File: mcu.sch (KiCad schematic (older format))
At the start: 16 parts, among them SW3 SW_PUSH, U1 STM32F411RE_LQFP64, X1 32.768K, X2 8MHz

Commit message: Began layout
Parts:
- removed C1, C2: 10pF, Capacitors_SMD:C_0805_HandSoldering, symbol C
- removed X1: 32.768K, Crystals:Crystal_HC49-SD_SMD, symbol CRYSTAL
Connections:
- wire segments 111 -> 103
- no-connect marks 17 -> 19
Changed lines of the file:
@@
 USART_RX
-$Comp
-L CRYSTAL X1
-U 1 1 5430D2CD
-P 3150 1850
-F 0 "X1" H 3150 2000 60  0000 C CNN
-F 1 "32.768K" H 3150 1700 60  0000 C CNN
-F 2 "Crystals:Crystal_HC49-SD_SMD" H 3150 1850 60  0001 C CNN
-F 3 "~" H 3150 1850 60  0000 C CNN
-	1    3150 1850
-	0    1    1    0
-$EndComp
 $Comp
 L CRYSTAL X2
@@
 	1    3150 2800
 	0    1    1    0
-$EndComp
-$Comp
-L C C1
-U 1 1 5430D3C7
-P 2750 1500
-F 0 "C1" H 2750 1600 40  0000 L CNN
-F 1 "10pF" H 2756 1415 40  0000 L CNN
-F 2 "Capacitors_SMD:C_0805_HandSoldering" H 2788 1350 30  0000 C CNN
-F 3 "~" H 2750 1500 60  0000 C CNN
-	1    2750 1500
-	0    -1   -1   0
-$EndComp
-$Comp
-L C C2
-U 1 1 5430D401
-P 2750 2200
-F 0 "C2" H 2750 2300 40  0000 L CNN
-F 1 "10pF" H 2756 2115 40  0000 L CNN
-F 2 "Capacitors_SMD:C_0805_HandSoldering" H 2788 2050 30  0000 C CNN
-F 3 "~" H 2750 2200 60  0000 C CNN
-	1    2750 2200
-	0    -1   -1   0
 $EndComp
 $Comp
@@
 Connection ~ 7500 3400
 Wire Wire Line
-	2500 1500 2500 3250
-Wire Wire Line
-	2500 1500 2550 1500
-Wire Wire Line
-	2550 2200 2500 2200
-Connection ~ 2500 2200
-Wire Wire Line
 	2550 2450 2500 2450
 Connection ~ 2500 2450
@@
 Wire Wire Line
 	3150 2450 2950 2450
-Wire Wire Line
-	2950 2200 4450 2200
-Wire Wire Line
-	3150 2200 3150 2150
-Wire Wire Line
-	3150 1550 3150 1500
-Wire Wire Line
-	2950 1500 3500 1500
-Wire Wire Line
-	4450 2100 3500 2100
-Wire Wire Line
-	3500 2100 3500 1500
-Connection ~ 3150 1500
-Connection ~ 3150 2200
 Wire Wire Line
 	4450 2300 3150 2300
@@
 Text HLabel 7050 2600 2    60   Input ~ 0
 TRIGGER4
+Wire Wire Line
+	2500 3150 2500 2450
+NoConn ~ 4450 2100
+NoConn ~ 4450 2200
 $EndSCHEMATC

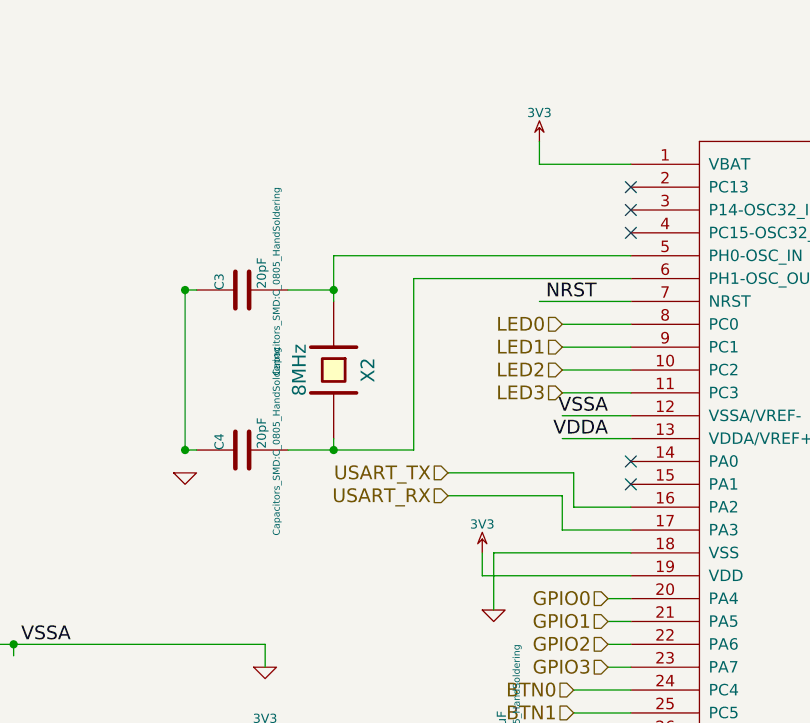
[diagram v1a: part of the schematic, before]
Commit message: New MOSFETs
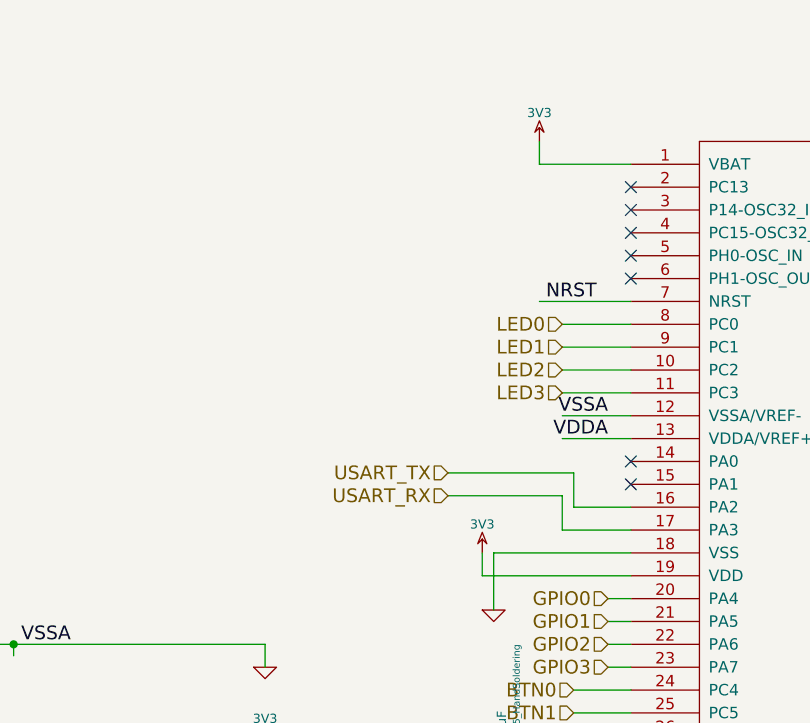
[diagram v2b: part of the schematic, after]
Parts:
- removed C3, C4: 20pF, Capacitors_SMD:C_0805_HandSoldering, symbol C
- removed X2: 8MHz, Crystals:Crystal_HC49-U_Vertical, symbol CRYSTAL
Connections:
- wire segments 103 -> 93
- no-connect marks 19 -> 21
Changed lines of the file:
@@
 LIBS:xbee
 LIBS:avbay-cache
-EELAYER 25 0
+EELAYER 27 0
 EELAYER END
 $Descr USLetter 11000 8500
@@
 Sheet 2 4
 Title "MCU"
-Date "4 dec 2014"
+Date "6 dec 2014"
 Rev ""
 Comp ""
@@
 $EndDescr
 $Comp
-L 3V3 #PWR08
+L 3V3 #PWR12
 U 1 1 542CDA8F
 P 3800 3600
-F 0 "#PWR08" H 3800 3700 40  0001 C CNN
+F 0 "#PWR12" H 3800 3700 40  0001 C CNN
 F 1 "3V3" H 3800 3725 40  0000 C CNN
 F 2 "" H 3800 3600 60  0000 C CNN
@@
 $EndComp
 $Comp
-L GND #PWR09
+L GND #PWR14
 U 1 1 542CDA9E
 P 3850 3850
-F 0 "#PWR09" H 3850 3850 30  0001 C CNN
+F 0 "#PWR14" H 3850 3850 30  0001 C CNN
 F 1 "GND" H 3850 3780 30  0001 C CNN
 F 2 "" H 3850 3850 60  0000 C CNN
@@
 $EndComp
 $Comp
-L 3V3 #PWR010
+L 3V3 #PWR13
 U 1 1 542CDAB1
 P 3800 4800
-F 0 "#PWR010" H 3800 4900 40  0001 C CNN
+F 0 "#PWR13" H 3800 4900 40  0001 C CNN
 F 1 "3V3" H 3800 4925 40  0000 C CNN
 F 2 "" H 3800 4800 60  0000 C CNN
@@
 $EndComp
 $Comp
-L 3V3 #PWR011
+L 3V3 #PWR22
 U 1 1 542CDAB7
 P 7450 4850
-F 0 "#PWR011" H 7450 4950 40  0001 C CNN
+F 0 "#PWR22" H 7450 4950 40  0001 C CNN
 F 1 "3V3" H 7450 4975 40  0000 C CNN
 F 2 "" H 7450 4850 60  0000 C CNN
@@
 $EndComp
 $Comp
-L 3V3 #PWR012
+L 3V3 #PWR23
 U 1 1 542CDC4D
 P 7500 3350
-F 0 "#PWR012" H 7500 3450 40  0001 C CNN
+F 0 "#PWR23" H 7500 3450 40  0001 C CNN
 F 1 "3V3" H 7500 3475 40  0000 C CNN
 F 2 "" H 7500 3350 60  0000 C CNN
@@
 Text HLabel 3650 3350 0    60   Input ~ 0
 USART_RX
-$Comp
-L CRYSTAL X2
-U 1 1 5430D2DC
-P 3150 2800
-F 0 "X2" H 3150 2950 60  0000 C CNN
-F 1 "8MHz" H 3150 2650 60  0000 C CNN
-F 2 "Crystals:Crystal_HC49-U_Vertical" H 3150 2800 60  0001 C CNN
-F 3 "~" H 3150 2800 60  0000 C CNN
-	1    3150 2800
-	0    1    1    0
-$EndComp
-$Comp
-L C C3
-U 1 1 5430D41B
-P 2750 2450
-F 0 "C3" H 2750 2550 40  0000 L CNN
-F 1 "20pF" H 2756 2365 40  0000 L CNN
-F 2 "Capacitors_SMD:C_0805_HandSoldering" H 2788 2300 30  0000 C CNN
-F 3 "~" H 2750 2450 60  0000 C CNN
-	1    2750 2450
-	0    -1   -1   0
-$EndComp
-$Comp
-L C C4
-U 1 1 5430D441
-P 2750 3150
-F 0 "C4" H 2750 3250 40  0000 L CNN
-F 1 "20pF" H 2756 3065 40  0000 L CNN
-F 2 "Capacitors_SMD:C_0805_HandSoldering" H 2788 3000 30  0000 C CNN
-F 3 "~" H 2750 3150 60  0000 C CNN
-	1    2750 3150
-	0    -1   -1   0
-$EndComp
-$Comp
-L GND #PWR013
-U 1 1 5430D447
-P 2500 3250
-F 0 "#PWR013" H 2500 3250 30  0001 C CNN
-F 1 "GND" H 2500 3180 30  0001 C CNN
-F 2 "" H 2500 3250 60  0000 C CNN
-F 3 "" H 2500 3250 60  0000 C CNN
-	1    2500 3250
-	1    0    0    -1
-$EndComp
 Text Label 5250 1100 2    60   ~ 0
 NRST
@@
 $EndComp
 $Comp
-L GND #PWR014
+L GND #PWR19
 U 1 1 5430D873
 P 6150 1450
-F 0 "#PWR014" H 6150 1450 30  0001 C CNN
+F 0 "#PWR19" H 6150 1450 30  0001 C CNN
 F 1 "GND" H 6150 1380 30  0001 C CNN
 F 2 "" H 6150 1450 60  0000 C CNN
@@
 $EndComp
 $Comp
-L 3V3 #PWR015
+L 3V3 #PWR24
 U 1 1 5430DC01
 P 7600 4350
-F 0 "#PWR015" H 7600 4450 40  0001 C CNN
+F 0 "#PWR24" H 7600 4450 40  0001 C CNN
 F 1 "3V3" H 7600 4475 40  0000 C CNN
 F 2 "" H 7600 4350 60  0000 C CNN
@@
 $EndComp
 $Comp
-L GND #PWR016
+L GND #PWR25
 U 1 1 5430DC07
 P 9000 4500
-F 0 "#PWR016" H 9000 4500 30  0001 C CNN
+F 0 "#PWR25" H 9000 4500 30  0001 C CNN
 F 1 "GND" H 9000 4430 30  0001 C CNN
 F 2 "" H 9000 4500 60  0000 C CNN
@@
 $EndComp
 $Comp
-L 3V3 #PWR017
+L 3V3 #PWR17
 U 1 1 5430E0CC
 P 5300 5450
-F 0 "#PWR017" H 5300 5550 40  0001 C CNN
+F 0 "#PWR17" H 5300 5550 40  0001 C CNN
 F 1 "3V3" H 5300 5575 40  0000 C CNN
 F 2 "" H 5300 5450 60  0000 C CNN
@@
 $EndComp
 $Comp
-L GND #PWR018
+L GND #PWR18
 U 1 1 5430E365
 P 5300 6050
-F 0 "#PWR018" H 5300 6050 30  0001 C CNN
+F 0 "#PWR18" H 5300 6050 30  0001 C CNN
 F 1 "GND" H 5300 5980 30  0001 C CNN
 F 2 "" H 5300 6050 60  0000 C CNN
@@
 $EndComp
 $Comp
-L GND #PWR019
+L GND #PWR11
 U 1 1 5430E5BA
 P 3550 4650
-F 0 "#PWR019" H 3550 4650 30  0001 C CNN
+F 0 "#PWR11" H 3550 4650 30  0001 C CNN
 F 1 "GND" H 3550 4580 30  0001 C CNN
 F 2 "" H 3550 4650 60  0000 C CNN
@@
 VDDA
 $Comp
-L 3V3 #PWR020
+L 3V3 #PWR15
 U 1 1 5430E17B
 P 4050 1800
-F 0 "#PWR020" H 4050 1900 40  0001 C CNN
+F 0 "#PWR15" H 4050 1900 40  0001 C CNN
 F 1 "3V3" H 4050 1925 40  0000 C CNN
 F 2 "" H 4050 1800 60  0000 C CNN
@@
 $EndComp
 $Comp
-L GND #PWR021
+L GND #PWR9
 U 1 1 5430E3DA
 P 2850 4100
-F 0 "#PWR021" H 2850 4100 30  0001 C CNN
+F 0 "#PWR9" H 2850 4100 30  0001 C CNN
 F 1 "GND" H 2850 4030 30  0001 C CNN
 F 2 "" H 2850 4100 60  0000 C CNN
@@
 $EndComp
 $Comp
-L 3V3 #PWR022
+L 3V3 #PWR10
 U 1 1 5430E3E0
 P 2850 4450
-F 0 "#PWR022" H 2850 4550 40  0001 C CNN
+F 0 "#PWR10" H 2850 4550 40  0001 C CNN
 F 1 "3V3" H 2850 4575 40  0000 C CNN
 F 2 "" H 2850 4450 60  0000 C CNN
@@
 	4150 3350 3650 3350
 Connection ~ 7500 3400
-Wire Wire Line
-	2550 2450 2500 2450
-Connection ~ 2500 2450
-Wire Wire Line
-	2550 3150 2500 3150
-Connection ~ 2500 3150
-Wire Wire Line
-	3150 3100 3150 3150
-Wire Wire Line
-	2950 3150 3500 3150
-Wire Wire Line
-	3150 2300 3150 2500
-Wire Wire Line
-	3150 2450 2950 2450
-Wire Wire Line
-	4450 2300 3150 2300
-Connection ~ 3150 2450
-Wire Wire Line
-	4450 2400 3500 2400
-Wire Wire Line
-	3500 2400 3500 3150
-Connection ~ 3150 3150
 Wire Wire Line
 	5550 1400 5350 1400
@@
 	4150 4900 4150 5300
 $Comp
-L GND #PWR023
+L GND #PWR16
 U 1 1 54449600
 P 4150 5300
-F 0 "#PWR023" H 4150 5300 30  0001 C CNN
+F 0 "#PWR16" H 4150 5300 30  0001 C CNN
 F 1 "GND" H 4150 5230 30  0001 C CNN
 F 2 "" H 4150 5300 60  0000 C CNN
@@
 	7350 4900 7350 5100
 $Comp
-L GND #PWR024
+L GND #PWR20
 U 1 1 5444A762
 P 7350 3600
-F 0 "#PWR024" H 7350 3600 30  0001 C CNN
+F 0 "#PWR20" H 7350 3600 30  0001 C CNN
 F 1 "GND" H 7350 3530 30  0001 C CNN
 F 2 "" H 7350 3600 60  0000 C CNN
@@
 	7350 3300 7350 3600
 $Comp
-L GND #PWR025
+L GND #PWR21
 U 1 1 54449656
 P 7350 5100
-F 0 "#PWR025" H 7350 5100 30  0001 C CNN
+F 0 "#PWR21" H 7350 5100 30  0001 C CNN
 F 1 "GND" H 7350 5030 30  0001 C CNN
 F 2 "" H 7350 5100 60  0000 C CNN
@@
 Text HLabel 7050 2600 2    60   Input ~ 0
 TRIGGER4
-Wire Wire Line
-	2500 3150 2500 2450
 NoConn ~ 4450 2100
 NoConn ~ 4450 2200
+NoConn ~ 4450 2300
+NoConn ~ 4450 2400
 $EndSCHEMATC
